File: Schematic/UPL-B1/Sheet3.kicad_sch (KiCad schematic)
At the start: 103 parts, among them P30 TestPoint, P31 TestPoint, P32 TestPoint, P33 TestPoint, P34 TestPoint

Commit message: Add device datasheets, begin migration to hierarchical labels
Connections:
- net FRQ RG1 renamed FRQ_RG1
- net FRQ RG2 renamed FRQ_RG2
- net FRQ RG3 renamed FRQ_RG3
- net ~{WR} renamed /WR
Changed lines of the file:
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@@
 		)
 	)
-	(global_label "SD1"
-		(shape input)
-		(at 83.82 304.8 180)
-		(fields_autoplaced yes)
-		(effects
-			(font
-				(size 1.27 1.27)
-			)
-			(justify right)
-		)
-		(property "Intersheetrefs" "${INTERSHEET_REFS}"
-			(at 77.1458 304.8 0)
-			(effects
-				(font
-					(size 1.27 1.27)
-				)
-				(justify right)
-				(hide yes)
-			)
-		)
-	)
 	(global_label "CLK"
 		(shape input)
@@
 		)
 	)
-	(global_label "SIN"
+	(global_label "WR"
 		(shape input)
-		(at 36.83 87.63 180)
+		(at 248.92 289.56 180)
 		(fields_autoplaced yes)
 		(effects
@@
 		)
 		(property "Intersheetrefs" "${INTERSHEET_REFS}"
-			(at 30.7 87.63 0)
+			(at 243.2134 289.56 0)
 			(effects
 				(font
@@
 		)
 	)
-	(global_label "WR"
+	(hierarchical_label "SD1"
 		(shape input)
-		(at 248.92 289.56 180)
-		(fields_autoplaced yes)
+		(at 83.82 304.8 180)
 		(effects
 			(font
@@
 			(justify right)
 		)
-		(property "Intersheetrefs" "${INTERSHEET_REFS}"
-			(at 243.2134 289.56 0)
-			(effects
-				(font
-					(size 1.27 1.27)
-				)
-				(justify right)
-				(hide yes)
-			)
-		)
 	)
-	(global_label "FRQ RG1"
+	(hierarchical_label "SIN"
 		(shape input)
-		(at 226.06 44.45 180)
-		(fields_autoplaced yes)
+		(at 36.83 87.63 180)
 		(effects
 			(font
@@
 			(justify right)
 		)
-		(property "Intersheetrefs" "${INTERSHEET_REFS}"
-			(at 214.6686 44.45 0)
-			(effects
-				(font
-					(size 1.27 1.27)
-				)
-				(justify right)
-				(hide yes)
-			)
-		)
 	)
-	(global_label "SD2"
+	(hierarchical_label "SD2"
 		(shape output)
 		(at 558.8 308.61 0)
-		(fields_autoplaced yes)
 		(effects
 			(font
@@
 			(justify left)
 		)
-		(property "Intersheetrefs" "${INTERSHEET_REFS}"
-			(at 565.4742 308.61 0)
-			(effects
-				(font
-					(size 1.27 1.27)
-				)
-				(justify left)
-				(hide yes)
-			)
-		)
 	)
-	(global_label "~{WR}"
-		(shape input)
-		(at 139.7 307.34 0)
-		(fields_autoplaced yes)
-		(effects
-			(font
-				(size 1.27 1.27)
-			)
-			(justify left)
-		)
-		(property "Intersheetrefs" "${INTERSHEET_REFS}"
-			(at 145.4066 307.34 0)
-			(effects
-				(font
-					(size 1.27 1.27)
-				)
-				(justify left)
-				(hide yes)
-			)
-		)
-	)
-	(global_label "CLK"
+	(hierarchical_label "CLK"
 		(shape input)
 		(at 426.72 297.18 180)
-		(fields_autoplaced yes)
 		(effects
 			(font
@@
 			(justify right)
 		)
-		(property "Intersheetrefs" "${INTERSHEET_REFS}"
-			(at 420.1667 297.18 0)
-			(effects
-				(font
-					(size 1.27 1.27)
-				)
-				(justify right)
-				(hide yes)
-			)
-		)
 	)
-	(global_label "COS"
+	(hierarchical_label "LOOP"
 		(shape output)
-		(at 387.35 153.67 0)
-		(fields_autoplaced yes)
+		(at 566.42 160.02 0)
 		(effects
 			(font
@@
 			(justify left)
 		)
-		(property "Intersheetrefs" "${INTERSHEET_REFS}"
-			(at 394.1452 153.67 0)
-			(effects
-				(font
-					(size 1.27 1.27)
-				)
-				(justify left)
-				(hide yes)
-			)
-		)
 	)
-	(global_label "FRQ RG3"
+	(hierarchical_label "FRQ_RG1"
 		(shape input)
-		(at 226.06 62.23 180)
-		(fields_autoplaced yes)
+		(at 226.06 44.45 180)
 		(effects
 			(font
@@
 			(justify right)
 		)
-		(property "Intersheetrefs" "${INTERSHEET_REFS}"
-			(at 214.6686 62.23 0)
-			(effects
-				(font
-					(size 1.27 1.27)
-				)
-				(justify right)
-				(hide yes)
-			)
-		)
 	)
-	(global_label "CLK"
+	(hierarchical_label "FRQ_RG3"
 		(shape input)
-		(at 83.82 307.34 180)
-		(fields_autoplaced yes)
+		(at 226.06 62.23 180)
 		(effects
 			(font
@@
 			(justify right)
 		)
-		(property "Intersheetrefs" "${INTERSHEET_REFS}"
-			(at 77.2667 307.34 0)
-			(effects
-				(font
-					(size 1.27 1.27)
-				)
-				(justify right)
-				(hide yes)
+	)
+	(hierarchical_label "COS"
+		(shape output)
+		(at 387.35 153.67 0)
+		(effects
+			(font
+				(size 1.27 1.27)
 			)
+			(justify left)
 		)
 	)
-	(global_label "ALC"
+	(hierarchical_label "ALC"
 		(shape output)
 		(at 566.42 110.49 0)
-		(fields_autoplaced yes)
 		(effects
 			(font
@@
 			(justify left)
 		)
-		(property "Intersheetrefs" "${INTERSHEET_REFS}"
-			(at 572.7919 110.49 0)
-			(effects
-				(font
-					(size 1.27 1.27)
-				)
-				(justify left)
-				(hide yes)
+	)
+	(hierarchical_label "CLK"
+		(shape input)
+		(at 83.82 307.34 180)
+		(effects
+			(font
+				(size 1.27 1.27)
 			)
+			(justify right)
 		)
 	)
-	(global_label "LOOP"
-		(shape output)
-		(at 566.42 160.02 0)
-		(fields_autoplaced yes)
+	(hierarchical_label "{slash}WR"
+		(shape input)
+		(at 139.7 307.34 0)
 		(effects
 			(font
@@
 			(justify left)
 		)
-		(property "Intersheetrefs" "${INTERSHEET_REFS}"
-			(at 574.3643 160.02 0)
-			(effects
-				(font
-					(size 1.27 1.27)
-				)
-				(justify left)
-				(hide yes)
-			)
-		)
 	)
-	(global_label "FRQ RG2"
+	(hierarchical_label "FRQ_RG2"
 		(shape input)
 		(at 226.06 53.34 180)
-		(fields_autoplaced yes)
 		(effects
 			(font
@@
 			(justify right)
 		)
-		(property "Intersheetrefs" "${INTERSHEET_REFS}"
-			(at 214.6686 53.34 0)
-			(effects
-				(font
-					(size 1.27 1.27)
-				)
-				(justify right)
-				(hide yes)
-			)
-		)
 	)
-	(global_label "~{WR}"
+	(hierarchical_label "{slash}WR"
 		(shape input)
 		(at 482.6 297.18 0)
-		(fields_autoplaced yes)
 		(effects
 			(font
@@
 			(justify left)
 		)
-		(property "Intersheetrefs" "${INTERSHEET_REFS}"
-			(at 488.3066 297.18 0)
-			(effects
-				(font
-					(size 1.27 1.27)
-				)
-				(justify left)
-				(hide yes)
-			)
-		)
 	)
 	(symbol
@@
 			)
 		)
-		(property "Datasheet" "~"
+		(property "Datasheet" "https://assets.nexperia.com/documents/data-sheet/BC859_BC860.pdf"
 			(at 92.71 167.64 0)
 			(effects
@@
 			)
 		)
-		(property "Datasheet" "~"
+		(property "Datasheet" "https://assets.nexperia.com/documents/data-sheet/BC859_BC860.pdf"
 			(at 92.71 208.28 0)
 			(effects
@@
 			)
 		)
-		(property "Datasheet" "~"
+		(property "Datasheet" "https://assets.nexperia.com/documents/data-sheet/BC859_BC860.pdf"
 			(at 92.71 132.08 0)
 			(effects
@@
 			)
 		)
-		(property "Datasheet" "https://ngspice.sourceforge.io/docs/ngspice-html-manual/manual.xhtml#cha_JFETs"
+		(property "Datasheet" "https://mm.digikey.com/Volume0/opasdata/d220001/medias/docus/906/J105%2C6%2C7.pdf"
 			(at 121.92 90.17 0)
 			(effects
@@
 			)
 		)
-		(property "Datasheet" "https://ngspice.sourceforge.io/docs/ngspice-html-manual/manual.xhtml#cha_JFETs"
+		(property "Datasheet" "https://www.nxp.com/docs/en/data-sheet/BSR56_57_58.pdf"
 			(at 121.92 160.02 0)
 			(effects
@@
 			)
 		)
-		(property "Datasheet" "https://ngspice.sourceforge.io/docs/ngspice-html-manual/manual.xhtml#cha_JFETs"
+		(property "Datasheet" "https://www.nxp.com/docs/en/data-sheet/BSR56_57_58.pdf"
 			(at 121.92 200.66 0)
 			(effects
@@
 			)
 		)
-		(property "Datasheet" "~"
+		(property "Datasheet" "https://assets.nexperia.com/documents/data-sheet/BC859_BC860.pdf"
 			(at 92.71 97.79 0)
 			(effects

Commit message: Cleanup component names
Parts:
- C300, C301, C309, C310, C311, C312: value 3p9 -> 3p9F
- C303: value 33n 63V 1% FKP -> 33nF 63V 1% FKP
- C304: value 2n2 100V 1% FKP -> 2n2F 100V 1% FKP
- C305: value 560p -> 560pF
- C319: value 3p3 -> 3p3F
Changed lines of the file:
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@@
 			)
 		)
-		(property "Value" "3p9"
+		(property "Value" "3p9F"
 			(at 135.89 283.2037 0)
 			(effects
@@
 			)
 		)
-		(property "Value" "3p9"
+		(property "Value" "3p9F"
 			(at 528.3263 275.59 90)
 			(effects
@@
 			)
 		)
-		(property "Value" "3p9"
+		(property "Value" "3p9F"
 			(at 194.3163 292.1 90)
 			(effects
@@
 			)
 		)
-		(property "Value" "33n 63V 1% FKP"
+		(property "Value" "33nF 63V 1% FKP"
 			(at 345.186 111.76 90)
 			(effects
@@
 			)
 		)
-		(property "Value" "3p9"
+		(property "Value" "3p9F"
 			(at 478.79 273.0437 0)
 			(effects
@@
 			)
 		)
-		(property "Value" "3p3"
+		(property "Value" "3p3F"
 			(at 471.17 128.016 90)
 			(effects
@@
 			)
 		)
-		(property "Value" "3p9"
+		(property "Value" "3p9F"
 			(at 532.13 116.586 90)
 			(effects
@@
 			)
 		)
-		(property "Value" "3p9"
+		(property "Value" "3p9F"
 			(at 528.3263 168.91 90)
 			(effects
@@
 			)
 		)
-		(property "Value" "2n2 100V 1% FKP"
+		(property "Value" "2n2F 100V 1% FKP"
 			(at 344.17 139.7 90)
 			(effects
@@
 			)
 		)
-		(property "Value" "560p"
+		(property "Value" "560pF"
 			(at 303.53 158.75 90)
 			(effects

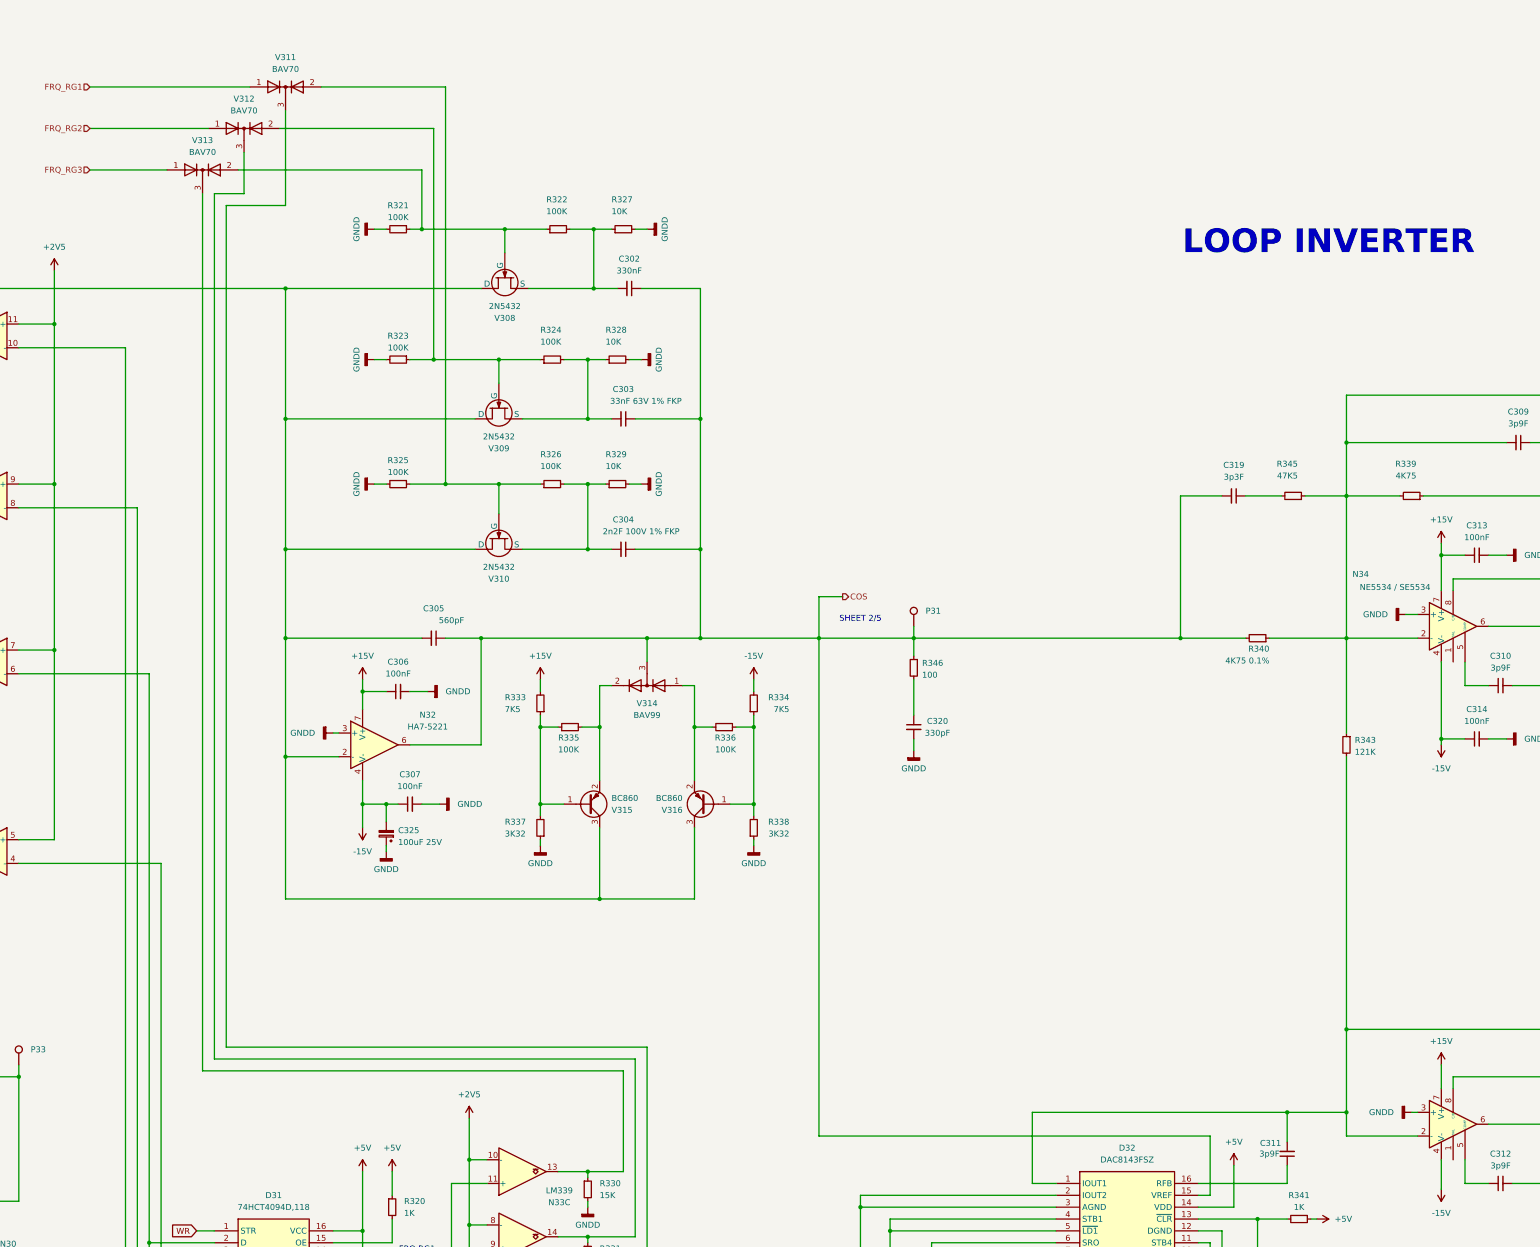
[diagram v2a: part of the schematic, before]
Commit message: Minor fixups for layout.
Reannotate, deduplicate N53B. Add some hierachical pins. First
preparations for layout
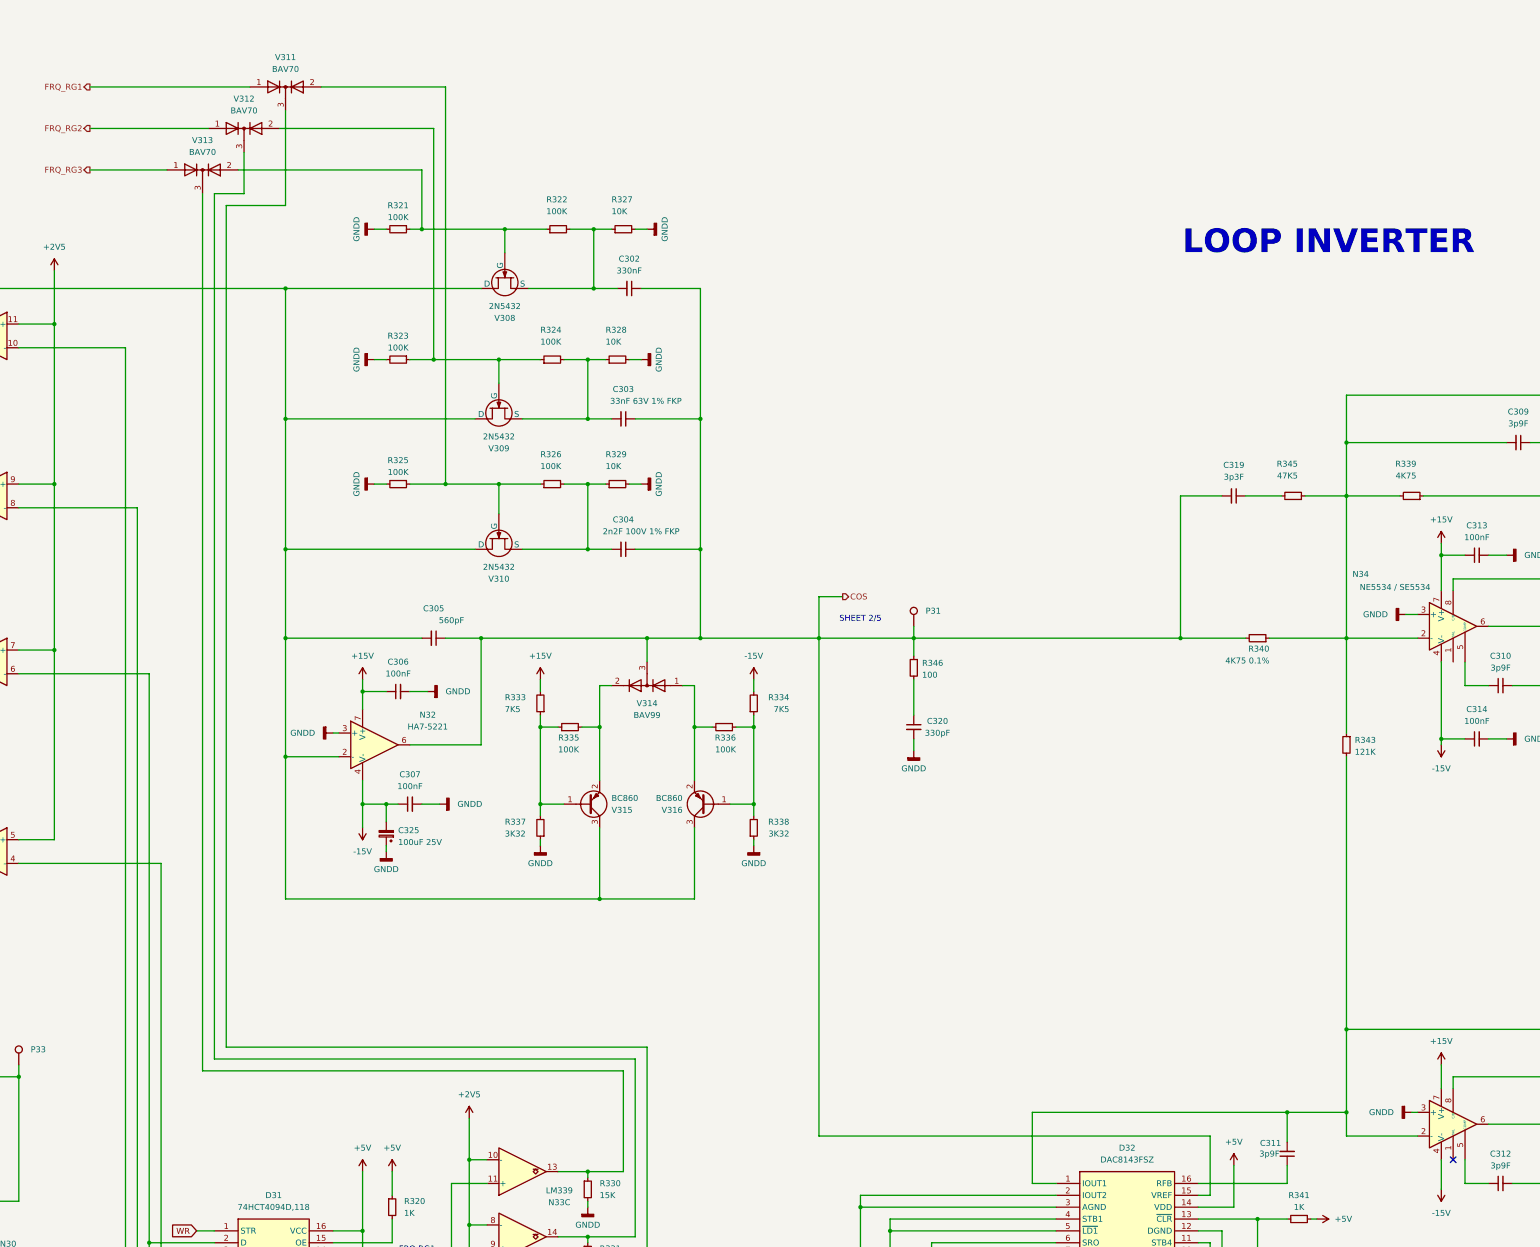
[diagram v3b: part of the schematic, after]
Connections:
- no-connect marks 0 -> 1
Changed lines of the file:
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@@
 		(color 0 0 0 0)
 	)
+	(no_connect
+		(at 518.16 274.32)
+	)
 	(wire
 		(pts
@@
 	)
 	(hierarchical_label "FRQ_RG1"
-		(shape input)
+		(shape output)
 		(at 226.06 44.45 180)
 		(effects
@@
 	)
 	(hierarchical_label "FRQ_RG3"
-		(shape input)
+		(shape output)
 		(at 226.06 62.23 180)
 		(effects
@@
 	)
 	(hierarchical_label "FRQ_RG2"
-		(shape input)
+		(shape output)
 		(at 226.06 53.34 180)
 		(effects

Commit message: Updated symbols for ADC and Shiftregister
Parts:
- D30, D32: symbol UPL_B1:DAC8143FSZ -> UPL_B1:DAC8143FSZ_
- D31: footprint 74HCT4094D118 -> Package_SO:SOIC-16_3.9x9.9mm_P1.27mm; symbol UPL_B1:74HCT4094D,118 -> UPL_B1:74HCT4094T-L
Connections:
- net at C300.2, N30.6, P33.1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: now also D30.16 (RFB); no longer D30.1 (IOUT1), N30.2 (-)
- net at C300.1: now also D30.1 (IOUT1), N30.2 (-); no longer D30.16 (RFB)
- net at D30.6 (SRO), D31.2 (D): no longer D31.5 (QP1), N31.6 (-)
- net at D32.1 (IOUT1), N35.2 (-), N35.6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: now also C311.1; no longer C311.2
- net at D32.16 (RFB): now also C311.2; no longer C311.1
- net /WR renamed ~{WR}
- new net: D31.5 (QP1), N31.6 (-)
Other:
- moved on the sheet: C300, C301, C302, C303, C304, C305, C306, C307, C308, C311, C312, C316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

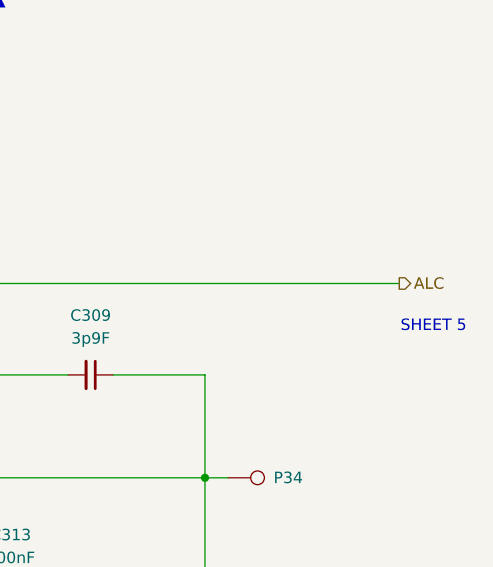
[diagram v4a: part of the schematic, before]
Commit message: Rework digital signal chain
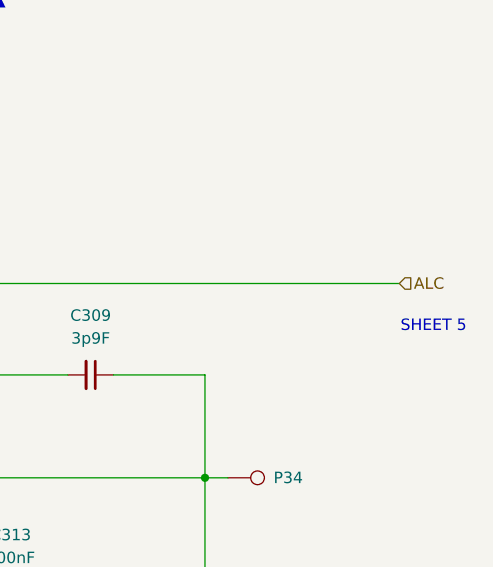
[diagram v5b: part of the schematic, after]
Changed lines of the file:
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@@
 	)
 	(hierarchical_label "ALC"
-		(shape output)
+		(shape input)
 		(at 566.42 110.49 0)
 		(effects

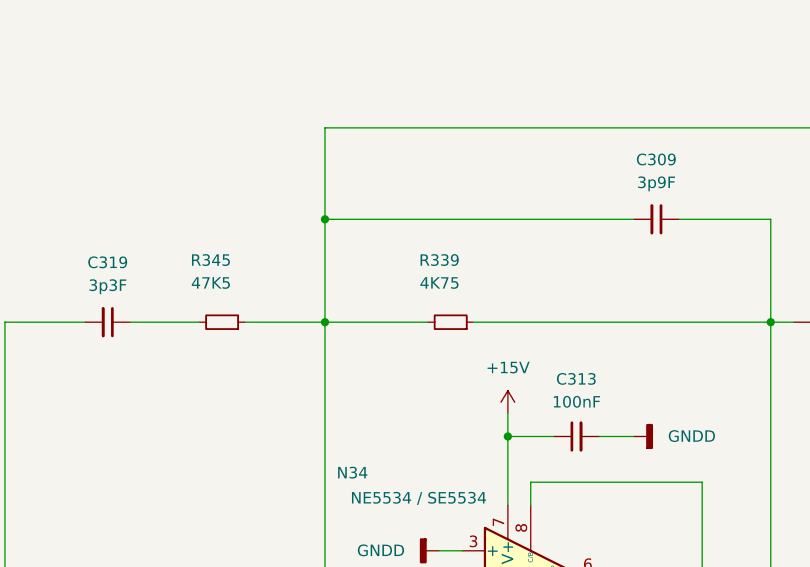
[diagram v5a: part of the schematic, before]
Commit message: added majority of footprints
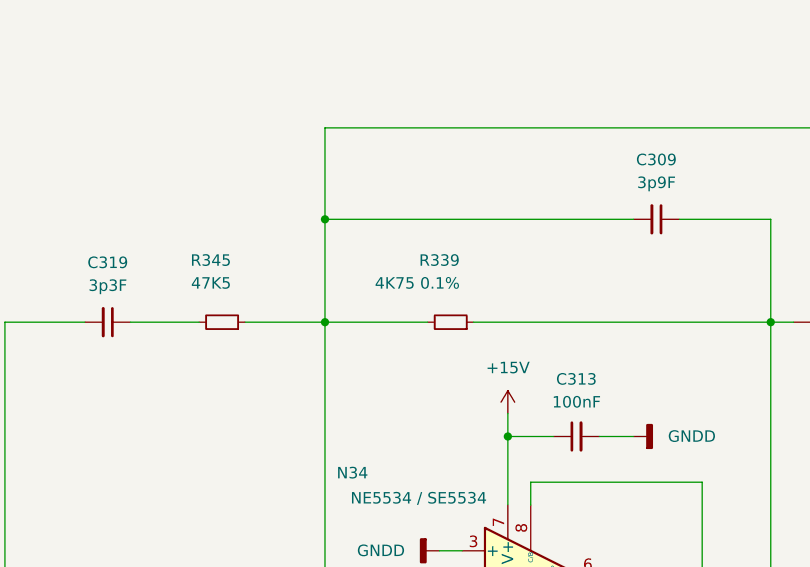
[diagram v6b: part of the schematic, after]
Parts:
- C300, C301, C305, C306, C307, C308, C309, C310, C311, C312, C313, C314, C316, C317, C319, C320, C321: footprint (none) -> Capacitor_SMD:C_1206_3216Metric_Pad1.33x1.80mm_HandSolder
- C302: footprint (none) -> Capacitor_THT:C_Axial_L22.0mm_D9.5mm_P27.50mm_Horizontal
- C315, C322, C325: footprint (none) -> Capacitor_THT:C_Radial_D6.3mm_H11.0mm_P2.50mm
- D30, D32: footprint SOIC127P1032X265-16N -> Package_SO:SOIC-16W_7.5x10.3mm_P1.27mm
- N30, N34, N35: footprint (none) -> Package_SO:SOIC-8_3.9x4.9mm_P1.27mm
- N31, N33: footprint (none) -> Package_SO:SOIC-14_3.9x8.7mm_P1.27mm
- P30, P31, P32, P33, P34: footprint (none) -> Connector_PinHeader_1.00mm:PinHeader_1x01_P1.00mm_Vertical
- R300, R302, R303, R304, R306, R308, R340: footprint (none) -> R_Axial_DIN0204_L3.6mm_D1.6mm_P7.62mm_Horizontal
- R301, R305, R307, R309, R310, R311, R312, R313, R314, R315, R316, R317, R318, R319, R320, R321, R322, R323, R324, R325, R326, R327, R328, R329, R330, R331, R332, R333, R334, R335, R336, R337, R338, R341, R342, R343, R344, R345, R346, R347, R348: footprint (none) -> Resistor_SMD:R_1206_3216Metric_Pad1.30x1.75mm_HandSolder
- R339: value 4K75 -> 4K75 0.1%; footprint (none) -> R_Axial_DIN0204_L3.6mm_D1.6mm_P7.62mm_Horizontal
- V300, V301, V302, V303, V305, V306, V307: footprint (none) -> Package_TO_SOT_SMD:SOT-23
- V304: footprint (none) -> Package_TO_SOT_THT:TO-92L_Inline
- V308, V309, V310: footprint (none) -> Package_TO_SOT_THT:TO-52-3

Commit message: Rough component outline on PCB
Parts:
- C302: footprint Capacitor_THT:C_Axial_L22.0mm_D9.5mm_P27.50mm_Horizontal -> Capacitor_THT:C_Axial_L17.0mm_D7.0mm_P25.00mm_Horizontal
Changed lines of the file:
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@@
 			)
 		)
-		(property "Footprint" "Capacitor_THT:C_Axial_L22.0mm_D9.5mm_P27.50mm_Horizontal"
+		(property "Footprint" "Capacitor_THT:C_Axial_L17.0mm_D7.0mm_P25.00mm_Horizontal"
 			(at 354.33 87.63 0)
 			(effects
